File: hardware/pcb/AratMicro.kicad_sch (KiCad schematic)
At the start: 0 parts

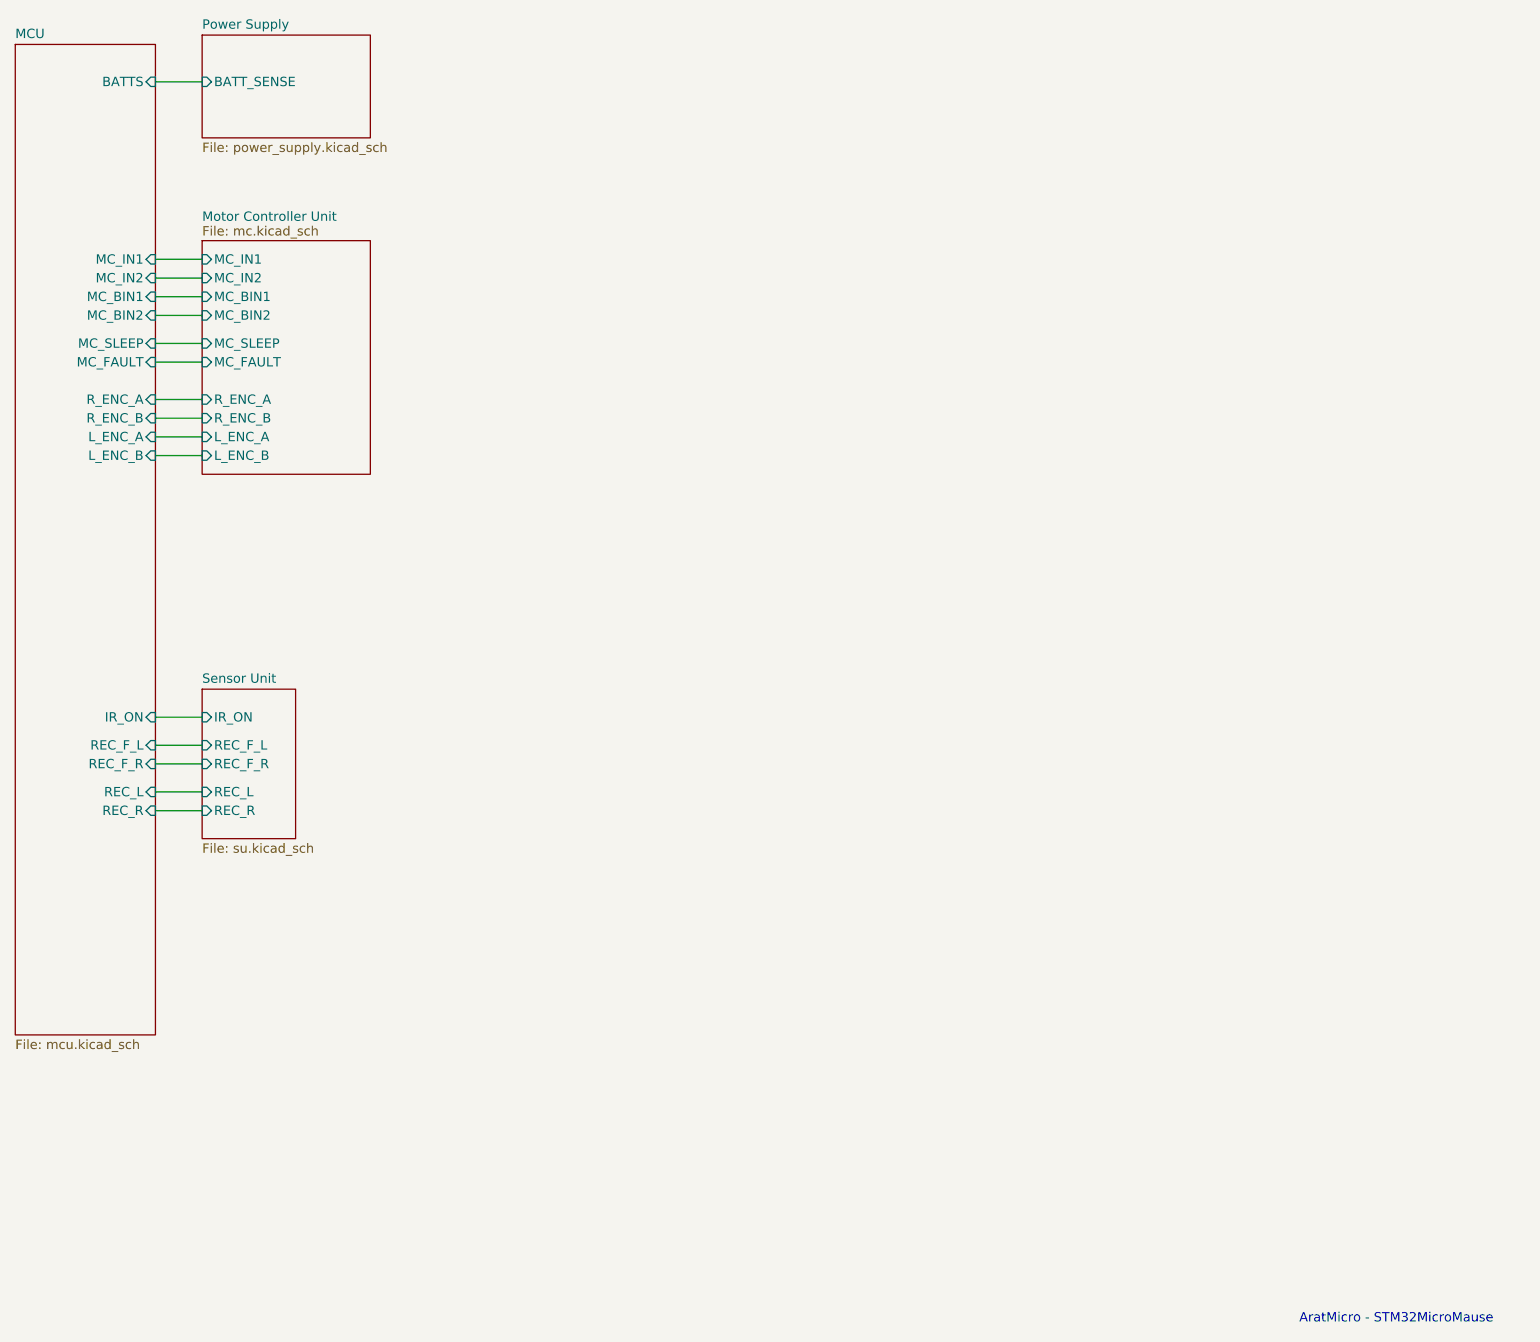
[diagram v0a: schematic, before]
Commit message: hardware: freeze schematic v1 after complete PCB redesign
Complete PCB and schematic refresh with reorganized sheets (psu, ui),
updated MCU/motor/sensor subsystems, and v1 schematic baseline frozen.
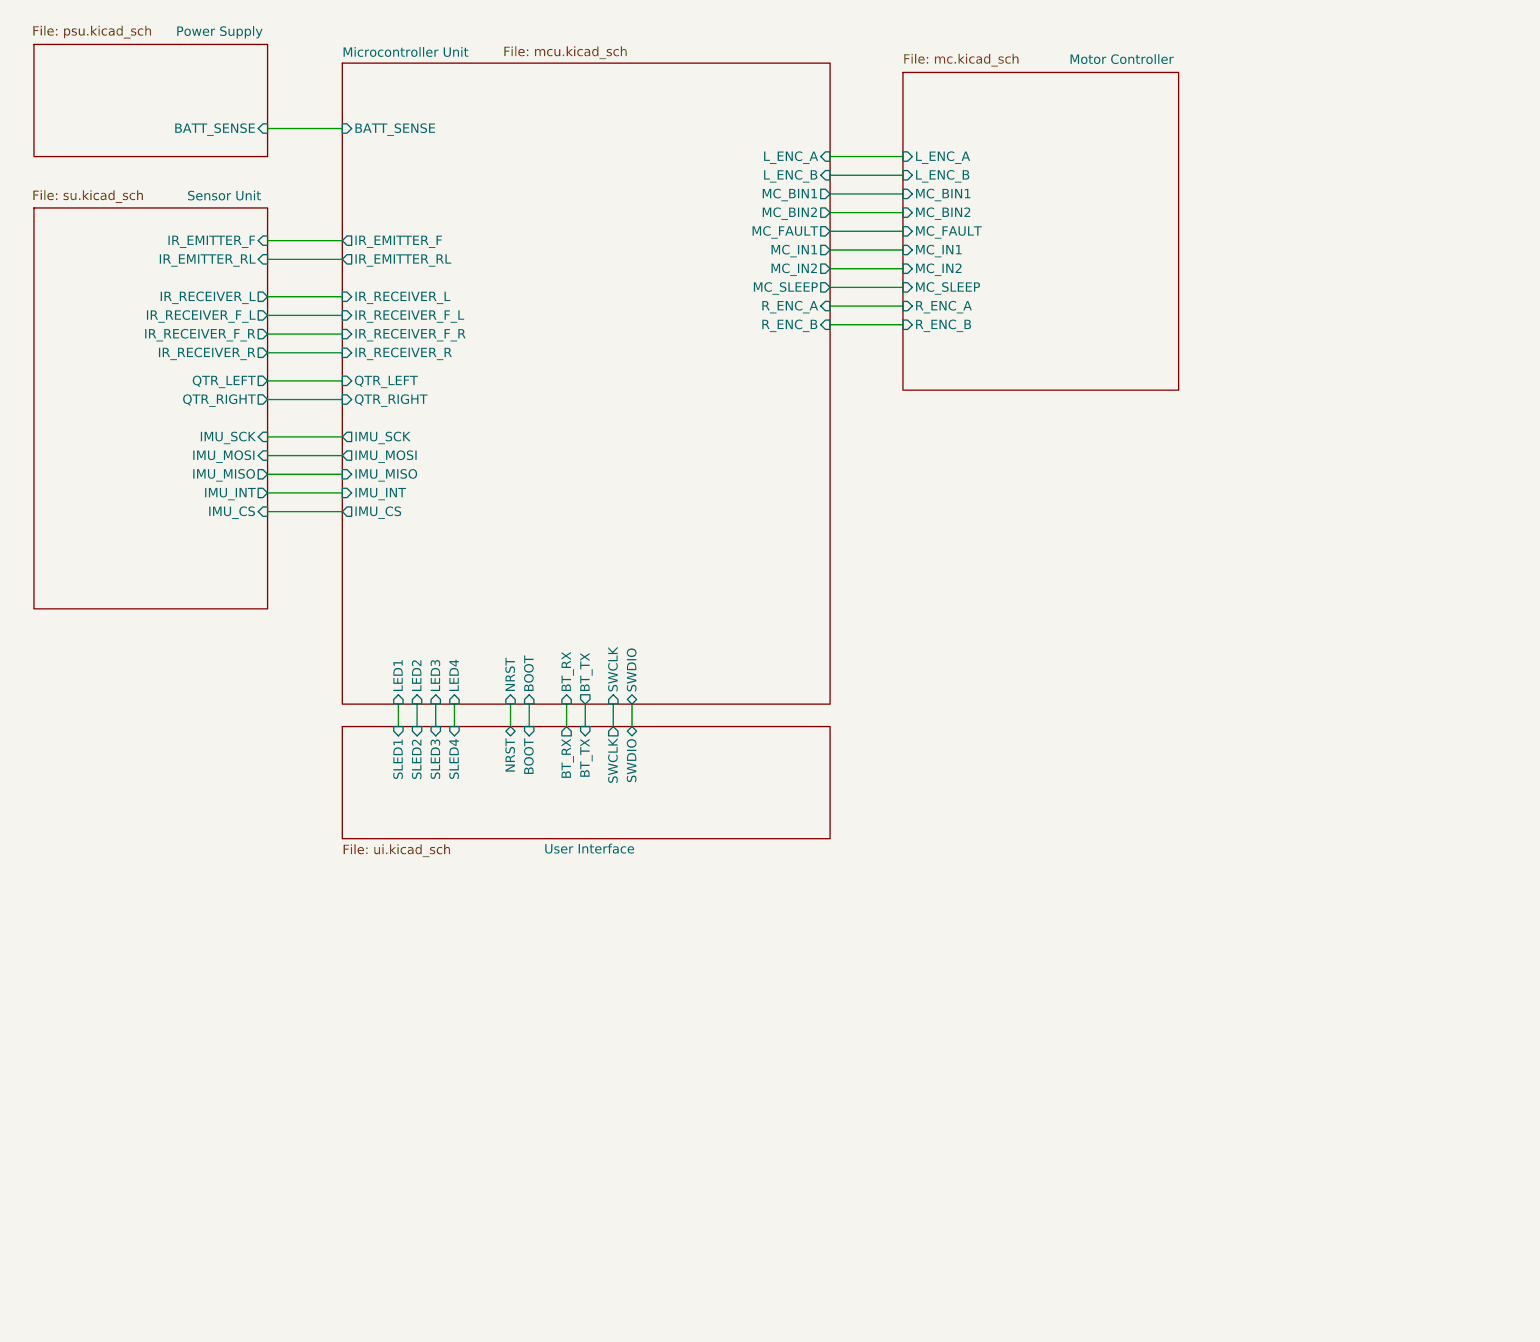
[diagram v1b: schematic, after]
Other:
- removed sheet MCU
- removed sheet Motor Controller Unit
- added sheet Microcontroller Unit (mcu.kicad_sch)
- added sheet Motor Controller (mc.kicad_sch)
- added sheet User Interface (ui.kicad_sch)
- sheet Power Supply: file power_supply.kicad_sch -> psu.kicad_sch
- sheet Sensor Unit ports: added IMU_CS, IMU_INT, IMU_MISO, IMU_MOSI, IMU_SCK, IR_EMITTER_F, IR_EMITTER_RL, IR_RECEIVER_F_L, IR_RECEIVER_F_R, IR_RECEIVER_L, IR_RECEIVER_R, QTR_LEFT, QTR_RIGHT; removed IR_ON, REC_F_L, REC_F_R, REC_L, REC_R
- note removed: "AratMicro - STM32MicroMause"
